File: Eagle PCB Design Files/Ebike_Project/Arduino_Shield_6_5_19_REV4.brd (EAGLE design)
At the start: 31.8 x 53.3 mm, 31 parts, among them IC1 FT232RL, IC2 LM1117IMPX-5.0, IC3 328P-MUR, SW1 RESET, Y1 16MHz

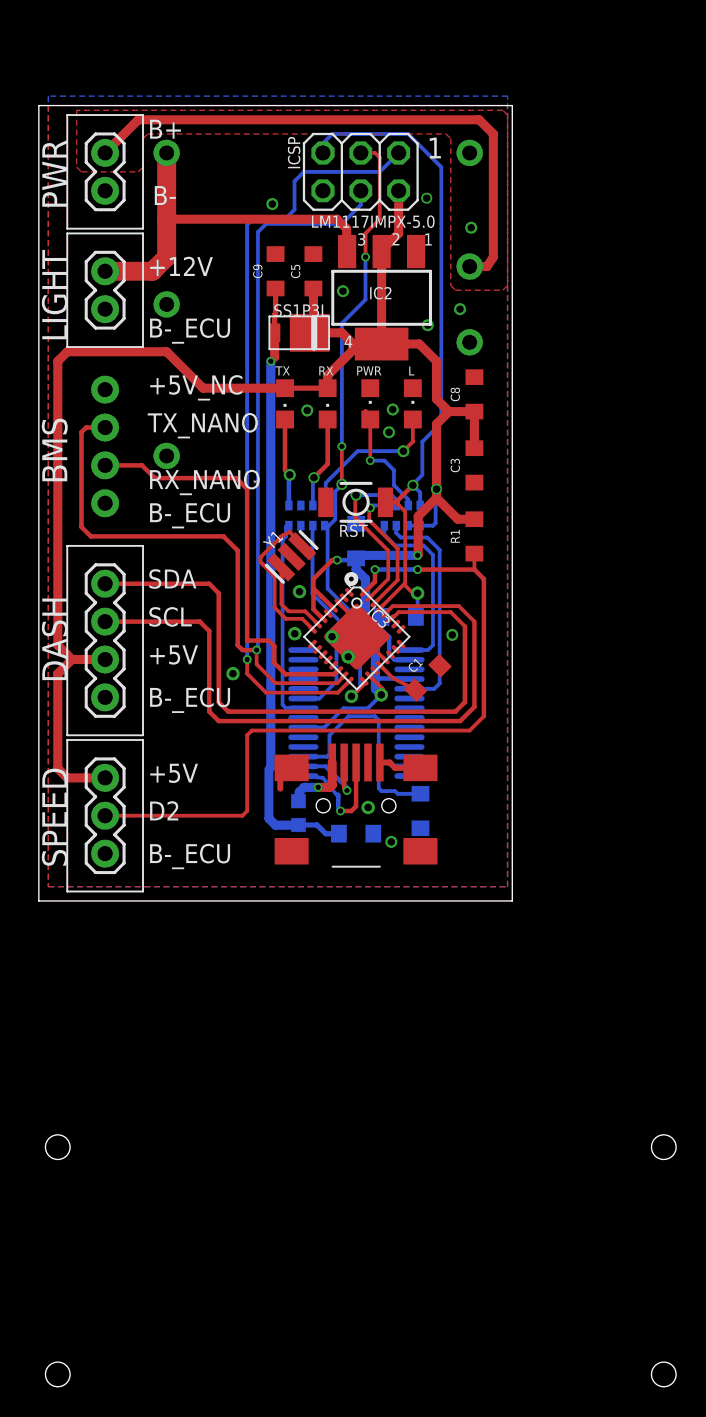
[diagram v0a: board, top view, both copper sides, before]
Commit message: REV4 is Complete, PCB and BOM sent out
Evaluation of REV4 will be completed by the end of July
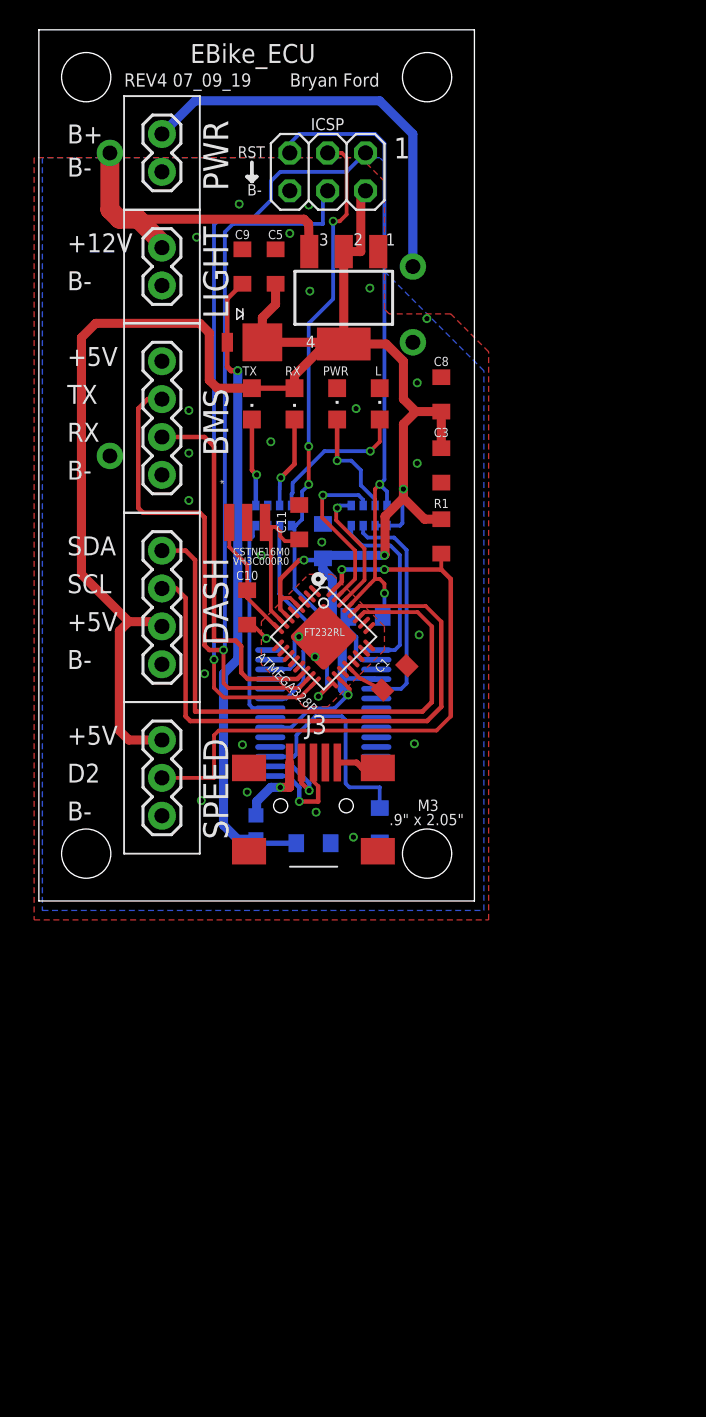
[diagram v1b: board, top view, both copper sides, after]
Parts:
- removed BMS1, DASH1: 4PIN_.1"_CONNECTOR, EBike_Project_Library:1X04
- removed HALL-SENSOR: 3PIN_.1"_CONNECTOR, EBike_Project_Library:1X03
- removed HEADLIGHT1, POWER: 2PIN_.1"_CONNECTOR, EBike_Project_Library:1X02
- removed SW1: RESET, Switches:SMD_157SW
- removed Y1: 16MHz, Cristalli:RESONATOR
- added C10, C11: 22pF, EBike_Project_Library:0805
- added CXTR_BMS, CXTR_DASH: 4PIN_.1"_CONNECTOR, EBike_Project_Library:1X04
- added CXTR_HALL_SENSOR: 3PIN_.1"_CONNECTOR, EBike_Project_Library:1X03
- added CXTR_HEADLIGHT, CXTR_POWER: 2PIN_.1"_CONNECTOR, EBike_Project_Library:1X02
- added RESONATOR: CSTNE16M0VH3C000R0, EBike_Project_Library:CRISTALLI_RESONATOR
- D1: device Diodi:DO220AAL -> EBike_Project_Library:SCHOTTKY_DIODE_DO220AAL
- F1: value MFFSMF050 -> MF-FSMF050X-2; device Arduino-rcl:0603-1608X90N -> EBike_Project_Library:0603
- IC1: device IntegratedCircuits:SSOP28 -> EBike_Project_Library:USB_SSOP28
- IC2: device IntegratedCircuits:LINEAR_SOT223 -> EBike_Project_Library:LINEAR_VREG_SOT223
- IC3: device Arduino-ucs&SoCs:VQFN32 -> EBike_Project_Library:VQFN32
- J3: value (none) -> UJ2-MBH-1-SMT-TR; device Connettori:USB-MINI-B_2 -> EBike_Project_Library:USB-MINI-B_2
- J4: device Connettori:2X03 -> EBike_Project_Library:2X03
- L: value Yellow -> Green; device Opto:CHIPLED_0805 -> EBike_Project_Library:LED_0805
- PWR, TX: device Opto:CHIPLED_0805 -> EBike_Project_Library:LED_0805
- R1: value 0.3 -> 4.99
- RP1, RP2: device Resistenze:CAY16 -> EBike_Project_Library:RESISTOR_ARRAY_CAY16
- RX: value Red -> Green; device Opto:CHIPLED_0805 -> EBike_Project_Library:LED_0805
- moved U$2 3.81 mm to (27.6, 52.7)
- moved D1 3.24 mm to (14.3, 37.5)
- moved F1 3.01 mm to (14.6, 4.94)
- moved C2 2.93 mm to (18.4, 3.87)
- moved C6 2.89 mm to (22.9, 5.08)
- moved J3 2.86 mm to (20.0, 9.28)
- moved C5 2.56 mm to (15.9, 42.5)
- moved IC2 2.54 mm to (20.4, 40.4)
- moved C9 2.25 mm to (13.7, 42.5)
- moved RP2 2.22 mm to (15.7, 25.8)
- moved TX 2.22 mm to (14.3, 33.3)
- moved C1 2.22 mm to (23.9, 15.0)
- moved C3 2.22 mm to (27.0, 29.2)
- moved C4 2.22 mm to (21.9, 19.1)
- moved C7 2.22 mm to (19.1, 24.1)
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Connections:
- removed net N$17: IC3.8, Y1.3
- new net N$20: C10.1, IC3.8, RESONATOR.3
- net +12V: now also CXTR_HEADLIGHT.2; no longer HEADLIGHT1.2
- net +5V: now also CXTR_DASH.2, CXTR_HALL_SENSOR.1; no longer DASH1.2, HALL-SENSOR.1
- net B+: now also CXTR_POWER.2; no longer POWER.2
- net B-_ECU: now also C10.2, C11.2, CXTR_BMS.4, CXTR_DASH.1, CXTR_HALL_SENSOR.3, CXTR_HEADLIGHT.1, CXTR_POWER.1, RESONATOR.2; no longer BMS1.4, DASH1.1, HALL-SENSOR.3, HEADLIGHT1.1, POWER.1, SW1.1, Y1.2
- net D2_HALL: now also CXTR_HALL_SENSOR.2; no longer HALL-SENSOR.2
- net LCD_SCL_BLUE_A5: now also CXTR_DASH.3; no longer DASH1.3
- net LCD_SDA_GREEN_A4: now also CXTR_DASH.4; no longer DASH1.4
- net N$14: now also C11.1, RESONATOR.1; no longer Y1.1
- net RESET: no longer SW1.2
- net RX_NANO_D10: now also CXTR_BMS.3; no longer BMS1.3
- net TX_NANO_D11: now also CXTR_BMS.2; no longer BMS1.2
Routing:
- net N$17: track 11.0 -> 0.00 mm
- net B+: track 37.5 -> 27.6 mm
- net N$20: track 0.00 -> 8.47 mm
- net D2_HALL: track 50.8 -> 42.6 mm
- net B-_ECU: track 14.9 -> 9.55 mm, vias 17 -> 27
- net N$14: track 5.47 -> 10.3 mm
- net RESET: track 48.1 -> 44.2 mm
- net LCD_SCL_BLUE_A5: track 43.4 -> 39.7 mm
- net LCD_SDA_GREEN_A4: track 42.9 -> 39.3 mm
- net +12V: track 25.4 -> 22.0 mm
- net RX_NANO_D10: track 28.2 -> 25.1 mm
- net TX_NANO_D11: track 71.2 -> 68.9 mm
- net VUSB: track 40.9 -> 43.1 mm
- net N$7: track 8.24 -> 7.23 mm
- net N$26: track 4.55 -> 5.22 mm
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- removed copper zone on layer 1, net HV_NC
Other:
- board size 31.8 x 53.3 mm -> 29.2 x 58.4 mm
- board text added: ".9" x 2.05""
- board text added: "ATMEGA328P"
- board text added: "CSTNE16M0"
- board text added: "EBike_ECU"
- board text added: "FT232RL"
- board text added: "M3"
- board text added: "REV4 07_09_19"
- board text added: "RX"
- board text added: "TX"
- board text added: "VH3C000R0"
- board text removed: "+5V_NC"
- board text removed: "B-_ECU"
- board text removed: "EBIKE SPEEDOMETER/BMS INTERFACE"
- board text removed: "REV3 6_21_19"
- board text removed: "RX_NANO"
- board text removed: "TX_NANO"

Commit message: Corrected polarity of DCDC converter of REV4 board
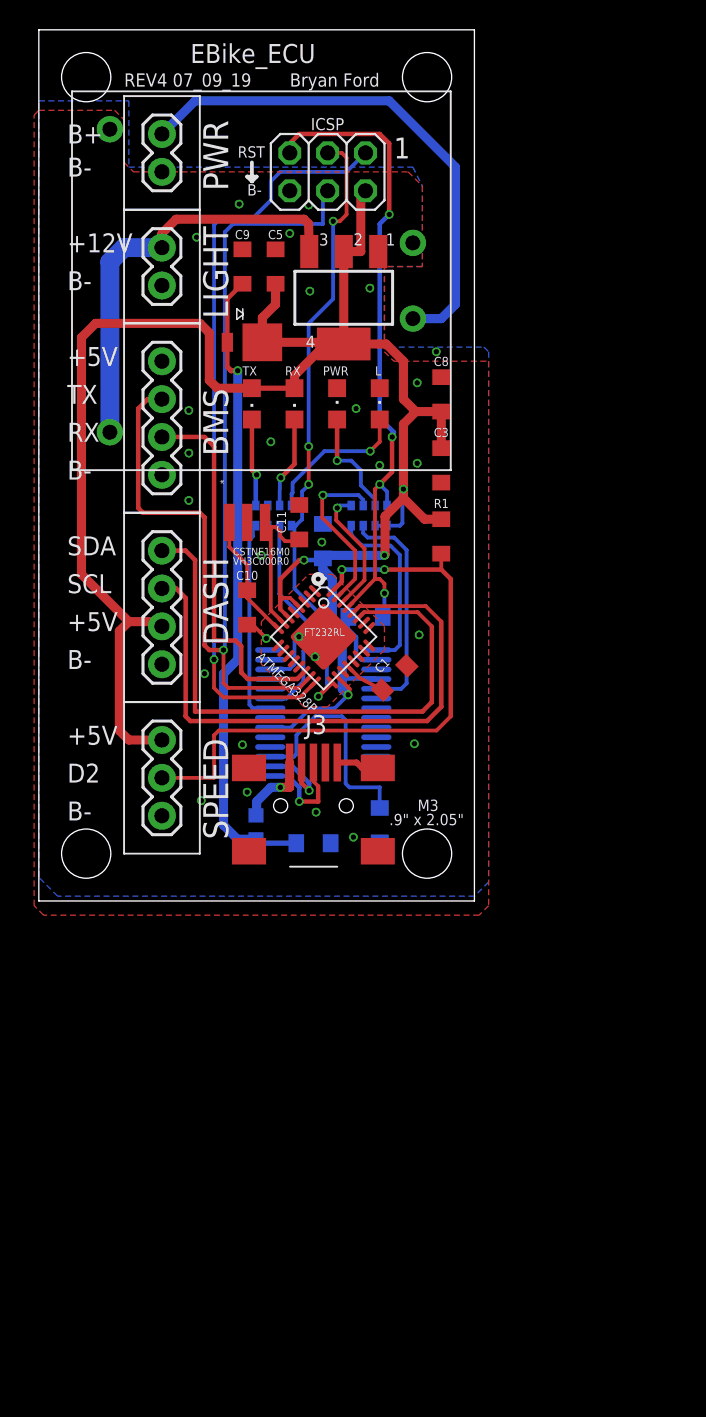
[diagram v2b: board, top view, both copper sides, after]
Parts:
- moved U$2 23.8 mm to (27.6, 28.9), flipped to the top, turned to 90 degrees
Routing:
- net B+: track 27.6 -> 34.9 mm
- net +12V: track 22.0 -> 28.5 mm
- net RESET: track 44.2 -> 45.4 mm, vias 2 -> 4
- net B-_ECU: vias 27 -> 28
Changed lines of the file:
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@@
 <attribute name="PRICE" value="0.1" x="26.9875" y="24.4475" size="1.778" layer="27" rot="R90" display="off"/>
 </element>
-<element name="U$2" library="EBike_Project_Library" package="SKM15C-12_DCDC" value="SKM15C-12_DCDC" x="27.6225" y="52.705" smashed="yes" rot="MR270">
-<attribute name="DESCRIPTION" value="Isolated DC/DC Converters 15W 36-75Vin 12Vout 125-1250mA 1x1 size" x="27.6225" y="52.705" size="1.778" layer="28" rot="MR270" display="off"/>
-<attribute name="LINK" value="https://www.mouser.com/ProductDetail/MEAN-WELL/SKM15C-12?qs=%2Fha2pyFaduhh55LLYaK%2FKJ2VcEvgwt5xUEx7a8eNZIE%3D" x="27.6225" y="52.705" size="1.778" layer="28" rot="MR270" display="off"/>
-<attribute name="PART_NUMBER" value=" SKM15C-12" x="27.6225" y="52.705" size="1.778" layer="28" rot="MR270" display="off"/>
-<attribute name="PRICE" value="25.44" x="27.6225" y="52.705" size="1.778" layer="28" rot="MR270" display="off"/>
+<element name="U$2" library="EBike_Project_Library" package="SKM15C-12_DCDC" value="SKM15C-12_DCDC" x="27.6225" y="28.8925" smashed="yes" rot="R90">
+<attribute name="DESCRIPTION" value="Isolated DC/DC Converters 15W 36-75Vin 12Vout 125-1250mA 1x1 size" x="27.6225" y="28.8925" size="1.778" layer="27" rot="R90" display="off"/>
+<attribute name="LINK" value="https://www.mouser.com/ProductDetail/MEAN-WELL/SKM15C-12?qs=%2Fha2pyFaduhh55LLYaK%2FKJ2VcEvgwt5xUEx7a8eNZIE%3D" x="27.6225" y="28.8925" size="1.778" layer="27" rot="R90" display="off"/>
+<attribute name="PART_NUMBER" value=" SKM15C-12" x="27.6225" y="28.8925" size="1.778" layer="27" rot="R90" display="off"/>
+<attribute name="PRICE" value="25.44" x="27.6225" y="28.8925" size="1.778" layer="27" rot="R90" display="off"/>
 </element>
 <element name="CXTR_DASH" library="EBike_Project_Library" package="1X04" value="4PIN_.1&quot;_CONNECTOR" x="8.255" y="15.875" smashed="yes" rot="R90">
@@
 <contactref element="CXTR_HEADLIGHT" pad="2"/>
 <contactref element="U$2" pad="+VOUT"/>
-<wire x1="6.6675" y1="45.72" x2="8.255" y2="44.1325" width="1.27" layer="1"/>
-<wire x1="8.255" y1="44.1325" x2="8.255" y2="43.815" width="1.27" layer="1"/>
-<wire x1="6.6675" y1="45.72" x2="17.78" y2="45.72" width="0.6096" layer="1"/>
+<wire x1="17.78" y1="45.72" x2="9.2075" y2="45.72" width="0.6096" layer="1"/>
 <wire x1="17.78" y1="45.72" x2="18.089428125" y2="45.410571875" width="0.6096" layer="1"/>
 <wire x1="18.089428125" y1="45.410571875" x2="18.1356" y2="43.5483" width="0.6096" layer="1"/>
-<wire x1="4.7625" y1="46.355" x2="5.3975" y2="45.72" width="1.27" layer="1"/>
-<wire x1="5.3975" y1="45.72" x2="6.6675" y2="45.72" width="1.27" layer="1"/>
-<wire x1="4.7625" y1="50.165" x2="4.7625" y2="46.355" width="1.27" layer="1"/>
+<wire x1="4.7625" y1="31.4325" x2="4.7625" y2="42.8625" width="1.27" layer="16"/>
+<wire x1="4.7625" y1="42.8625" x2="5.715" y2="43.815" width="1.27" layer="16"/>
+<wire x1="5.715" y1="43.815" x2="8.255" y2="43.815" width="1.27" layer="16"/>
+<wire x1="9.2075" y1="45.72" x2="8.255" y2="44.7675" width="0.6096" layer="1"/>
+<wire x1="8.255" y1="44.7675" x2="8.255" y2="43.815" width="0.6096" layer="1"/>
 </signal>
 <signal name="B-_ECU">
@@
 <contactref element="IC2" pad="1"/>
 <via x="15.5575" y="30.7975" extent="1-16" drill="0.35" diameter="0.6"/>
-<via x="26.0223" y="39.0525" extent="1-16" drill="0.35" diameter="0.6"/>
+<via x="26.6573" y="36.83" extent="1-16" drill="0.35" diameter="0.6"/>
 <via x="21.0947" y="4.2799" extent="1-16" drill="0.35" diameter="0.6"/>
 <contactref element="IC3" pad="21"/>
@@
 <via x="10.8966" y="6.731" extent="1-16" drill="0.35" diameter="0.6"/>
 <via x="10.5791" y="44.5135" extent="1-16" drill="0.35" diameter="0.6"/>
-<polygon width="0.6096" layer="16" isolate="0.1778">
-<vertex x="0.238125" y="-0.635"/>
-<vertex x="29.845" y="-0.635"/>
-<vertex x="29.845" y="35.56"/>
-<vertex x="23.1775" y="42.2275"/>
-<vertex x="23.1775" y="49.53"/>
-<vertex x="22.86" y="49.8475"/>
-<vertex x="0.238125" y="49.8475"/>
-</polygon>
 <wire x1="15.5194" y1="15.5275" x2="15.5494" y2="15.5575" width="0.254" layer="16"/>
 <wire x1="15.5494" y1="15.5575" x2="16.8275" y2="15.5575" width="0.254" layer="16"/>
@@
 <vertex x="14.9225" y="15.875"/>
 </polygon>
-<polygon width="0.254" layer="1" isolate="0.254">
-<vertex x="-0.3175" y="-1.27"/>
-<vertex x="30.1625" y="-1.27"/>
-<vertex x="30.1625" y="36.83"/>
-<vertex x="27.6225" y="39.37"/>
-<vertex x="23.495" y="39.37"/>
-<vertex x="23.1775" y="39.6875"/>
-<vertex x="23.1775" y="48.26"/>
-<vertex x="21.59" y="49.8475"/>
-<vertex x="-0.3175" y="49.8475"/>
-</polygon>
 <via x="14.9225" y="23.1775" extent="1-16" drill="0.35" diameter="0.6"/>
 <via x="13.6525" y="10.4775" extent="1-16" drill="0.35" diameter="0.6"/>
+<polygon width="0.6096" layer="16">
+<vertex x="0" y="53.6575"/>
+<vertex x="6.0325" y="53.6575"/>
+<vertex x="6.0325" y="49.2125"/>
+<vertex x="25.0825" y="49.2125"/>
+<vertex x="25.7175" y="47.9425"/>
+<vertex x="25.7175" y="42.545"/>
+<vertex x="23.1775" y="42.545"/>
+<vertex x="23.1775" y="37.465"/>
+<vertex x="23.495" y="37.1475"/>
+<vertex x="29.845" y="37.1475"/>
+<vertex x="30.1625" y="36.83"/>
+<vertex x="30.1625" y="1.27"/>
+<vertex x="29.21" y="0.3175"/>
+<vertex x="1.27" y="0.3175"/>
+<vertex x="0" y="1.5875"/>
+</polygon>
+<polygon width="0.6096" layer="1">
+<vertex x="0" y="53.0225"/>
+<vertex x="5.08" y="53.0225"/>
+<vertex x="5.715" y="52.3875"/>
+<vertex x="5.715" y="49.53"/>
+<vertex x="6.35" y="48.895"/>
+<vertex x="10.16" y="48.895"/>
+<vertex x="24.765" y="48.895"/>
+<vertex x="25.7175" y="47.9425"/>
+<vertex x="25.7175" y="42.545"/>
+<vertex x="23.1775" y="42.545"/>
+<vertex x="23.1775" y="36.83"/>
+<vertex x="23.8125" y="36.195"/>
+<vertex x="30.1625" y="36.195"/>
+<vertex x="30.1625" y="-0.3175"/>
+<vertex x="29.5275" y="-0.9525"/>
+<vertex x="0.3175" y="-0.9525"/>
+<vertex x="-0.3175" y="-0.3175"/>
+<vertex x="-0.3175" y="52.705"/>
+</polygon>
+<via x="22.86" y="29.21" extent="1-16" drill="0.35" diameter="0.6"/>
 </signal>
 <signal name="+5V">
@@
 <wire x1="23.3488" y1="27.4512" x2="22.86" y2="27.94" width="0.254" layer="16"/>
 <via x="23.1775" y="20.6375" extent="1-16" drill="0.35" diameter="0.6"/>
-<wire x1="16.8275" y1="50.165" x2="16.8275" y2="50.8" width="0.254" layer="16"/>
-<wire x1="17.4625" y1="51.435" x2="22.5425" y2="51.435" width="0.254" layer="16"/>
-<wire x1="22.5425" y1="51.435" x2="23.1775" y2="50.8" width="0.254" layer="16"/>
-<wire x1="23.1775" y1="28.2575" x2="23.1775" y2="50.8" width="0.254" layer="16"/>
-<wire x1="16.8275" y1="50.8" x2="17.4625" y2="51.435" width="0.254" layer="16"/>
-<wire x1="23.1775" y1="28.2575" x2="22.86" y2="27.94" width="0.254" layer="16"/>
 <wire x1="23.0615" y1="19.05" x2="23.1775" y2="19.685" width="0.254" layer="16"/>
 <wire x1="23.1775" y1="19.685" x2="23.1775" y2="20.6375" width="0.254" layer="16"/>
@@
 <wire x1="22.86" y1="27.94" x2="22.5425" y2="27.6225" width="0.254" layer="1"/>
 <wire x1="22.5425" y1="27.6225" x2="22.5425" y2="21.59" width="0.254" layer="1"/>
+<wire x1="23.495" y1="46.0375" x2="22.86" y2="45.4025" width="0.3048" layer="16"/>
+<via x="23.495" y="46.0375" extent="1-16" drill="0.35"/>
+<wire x1="23.495" y1="46.0375" x2="23.495" y2="50.8" width="0.3048" layer="1"/>
+<wire x1="23.495" y1="50.8" x2="22.86" y2="51.435" width="0.3048" layer="1"/>
+<wire x1="22.86" y1="51.435" x2="17.4625" y2="51.435" width="0.3048" layer="1"/>
+<wire x1="17.4625" y1="51.435" x2="16.8275" y2="50.8" width="0.3048" layer="1"/>
+<wire x1="16.8275" y1="50.8" x2="16.8275" y2="50.165" width="0.3048" layer="1"/>
+<wire x1="22.86" y1="45.4025" x2="22.86" y2="32.385" width="0.3048" layer="16"/>
+<wire x1="22.86" y1="32.385" x2="23.8125" y2="31.4325" width="0.3048" layer="16"/>
+<wire x1="23.8125" y1="31.4325" x2="23.6883" y2="31.3083" width="0.3048" layer="16"/>
+<wire x1="23.6883" y1="31.3083" x2="23.6883" y2="31.115" width="0.3048" layer="16"/>
+<via x="23.6883" y="31.115" extent="1-16" drill="0.35"/>
+<wire x1="23.6883" y1="31.115" x2="23.6883" y2="28.7683" width="0.3048" layer="1"/>
+<wire x1="23.6883" y1="28.7683" x2="22.86" y2="27.94" width="0.3048" layer="1"/>
 </signal>
 <signal name="D1/TX">
@@
 <contactref element="U$2" pad="+VIN"/>
 <wire x1="10.4775" y1="53.6575" x2="8.255" y2="51.435" width="0.6096" layer="16"/>
-<wire x1="22.86" y1="53.6575" x2="25.0825" y2="51.435" width="0.6096" layer="16"/>
-<wire x1="25.0825" y1="51.435" x2="25.0825" y2="42.545" width="0.6096" layer="16"/>
-<wire x1="10.4775" y1="53.6575" x2="22.86" y2="53.6575" width="0.6096" layer="16"/>
+<wire x1="10.4775" y1="53.6575" x2="23.495" y2="53.6575" width="0.6096" layer="16"/>
+<wire x1="27.94" y1="40.005" x2="26.9875" y2="39.0525" width="0.6096" layer="16"/>
+<wire x1="26.9875" y1="39.0525" x2="25.0825" y2="39.0525" width="0.6096" layer="16"/>
+<wire x1="23.495" y1="53.6575" x2="27.94" y2="49.2125" width="0.6096" layer="16"/>
+<wire x1="27.94" y1="49.2125" x2="27.94" y2="40.005" width="0.6096" layer="16"/>
 </signal>
 <signal name="N$20">
